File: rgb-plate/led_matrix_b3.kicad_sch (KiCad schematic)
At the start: 32 parts

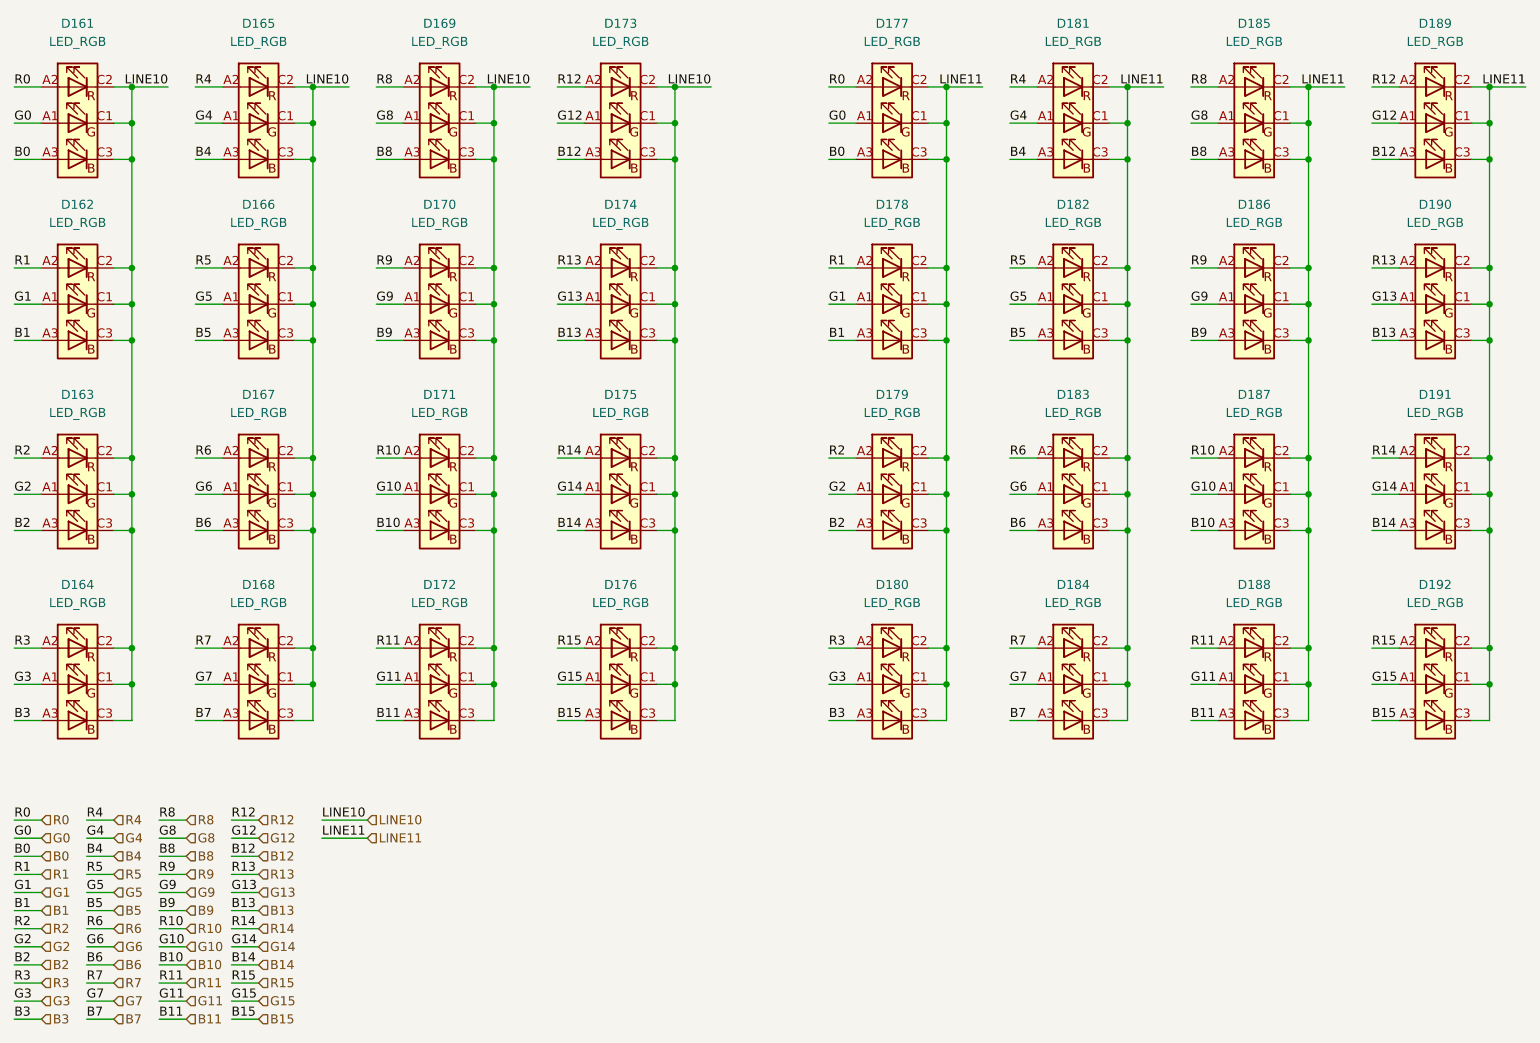
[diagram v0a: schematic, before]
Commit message: initial layout on single board, may need to split up
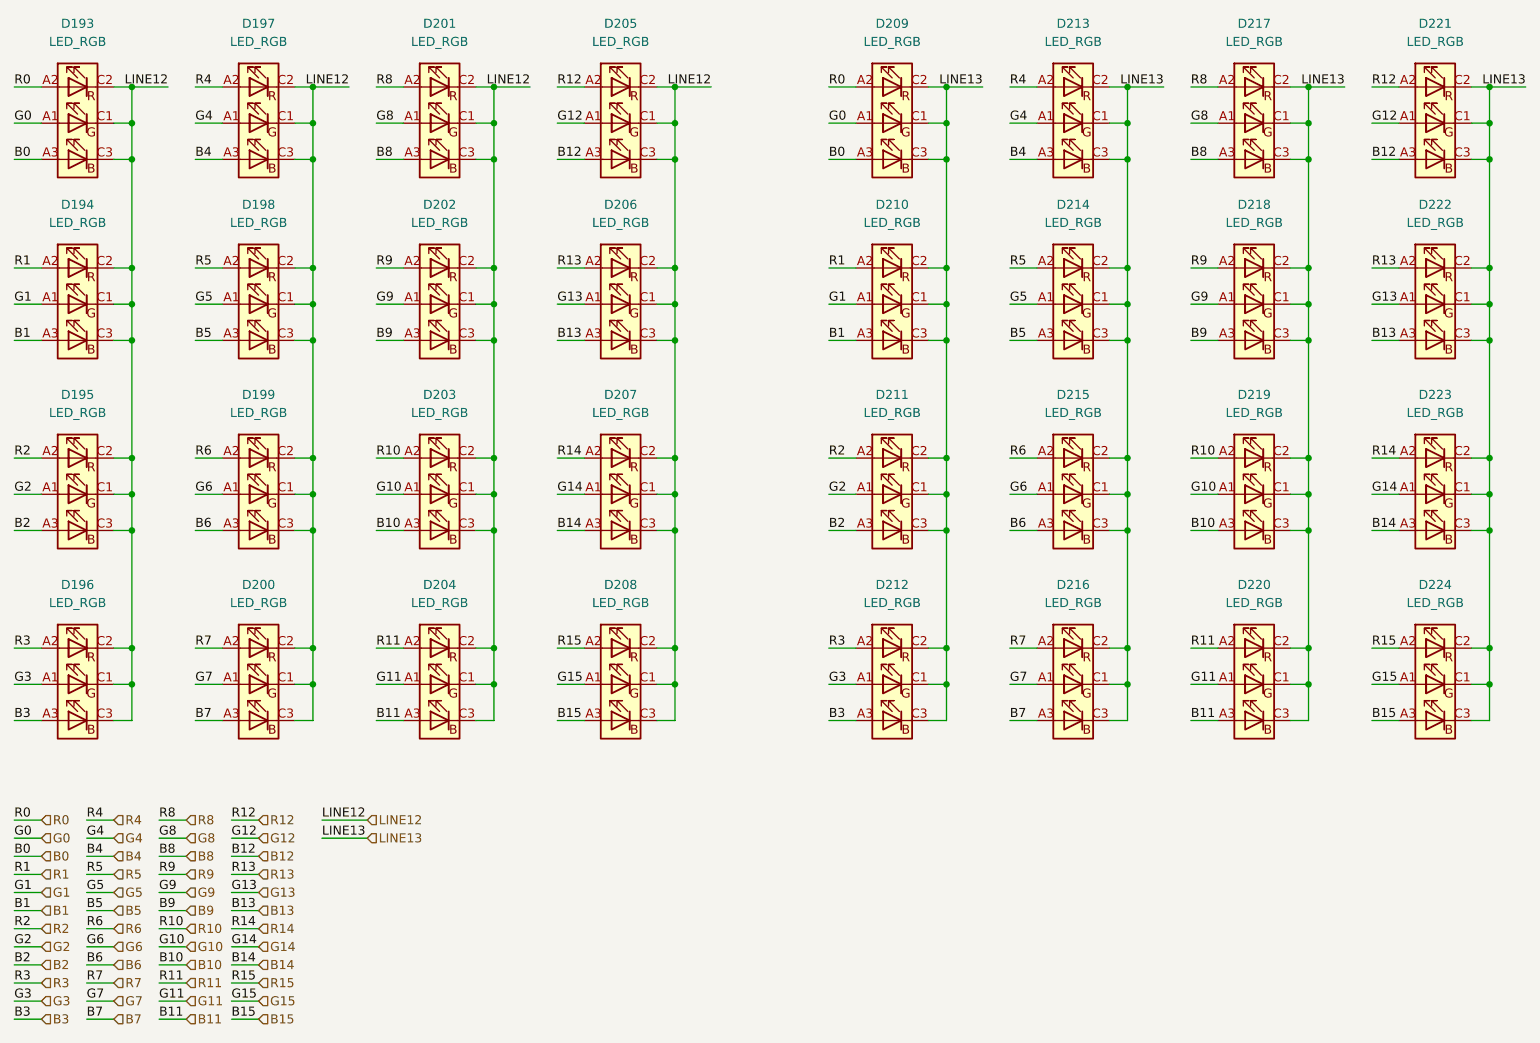
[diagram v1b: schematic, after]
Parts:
- removed D161, D162, D163, D164, D165, D166, D167, D168, D169, D170, D171, D172, D173, D174, D175, D176, D177, D178, D179, D180, D181, D182, D183, D184, D185, D186, D187, D188, D189, D190, D191, D192: LED_RGB, LRTBGVSR-4U4V-JW+8A8B-D8-3S4U-7Z:LRTBGVSR4U4VJW8A8BD83S4U7Z, symbol LRTBGVSR-4U4V-JW+8A8B-D8-3S4U-:LED_RGB
- added D193, D194, D195, D196, D197, D198, D199, D200, D201, D202, D203, D204, D205, D206, D207, D208, D209, D210, D211, D212, D213, D214, D215, D216, D217, D218, D219, D220, D221, D222, D223, D224: LED_RGB, LRTBGVSR-4U4V-JW+8A8B-D8-3S4U-7Z:LRTBGVSR4U4VJW8A8BD83S4U7Z, symbol LRTBGVSR-4U4V-JW+8A8B-D8-3S4U-:LED_RGB
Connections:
- net B0: now also D193.A3 (BA), D209.A3 (BA)
- net B1: now also D194.A3 (BA), D210.A3 (BA)
- net B10: now also D203.A3 (BA), D219.A3 (BA)
- net B11: now also D204.A3 (BA), D220.A3 (BA)
- net B12: now also D205.A3 (BA), D221.A3 (BA)
- net B13: now also D206.A3 (BA), D222.A3 (BA)
- net B14: now also D207.A3 (BA), D223.A3 (BA)
- net B15: now also D208.A3 (BA), D224.A3 (BA)
- net B2: now also D195.A3 (BA), D211.A3 (BA)
- net B3: now also D196.A3 (BA), D212.A3 (BA)
- net B4: now also D197.A3 (BA), D213.A3 (BA)
- net B5: now also D198.A3 (BA), D214.A3 (BA)
- net B6: now also D199.A3 (BA), D215.A3 (BA)
- net B7: now also D200.A3 (BA), D216.A3 (BA)
- net B8: now also D201.A3 (BA), D217.A3 (BA)
- net B9: now also D202.A3 (BA), D218.A3 (BA)
- net G0: now also D193.A1 (GA), D209.A1 (GA)
- net G1: now also D194.A1 (GA), D210.A1 (GA)
- net G10: now also D203.A1 (GA), D219.A1 (GA)
- net G11: now also D204.A1 (GA), D220.A1 (GA)
- net G12: now also D205.A1 (GA), D221.A1 (GA)
- net G13: now also D206.A1 (GA), D222.A1 (GA)
- net G14: now also D207.A1 (GA), D223.A1 (GA)
- net G15: now also D208.A1 (GA), D224.A1 (GA)
- net G2: now also D195.A1 (GA), D211.A1 (GA)
- net G3: now also D196.A1 (GA), D212.A1 (GA)
- net G4: now also D197.A1 (GA), D213.A1 (GA)
- net G5: now also D198.A1 (GA), D214.A1 (GA)
- net G6: now also D199.A1 (GA), D215.A1 (GA)
- net G7: now also D200.A1 (GA), D216.A1 (GA)
- net G8: now also D201.A1 (GA), D217.A1 (GA)
- net G9: now also D202.A1 (GA), D218.A1 (GA)
- net R0: now also D193.A2 (RA), D209.A2 (RA)
- net R1: now also D194.A2 (RA), D210.A2 (RA)
- net R10: now also D203.A2 (RA), D219.A2 (RA)
- net R11: now also D204.A2 (RA), D220.A2 (RA)
- net R12: now also D205.A2 (RA), D221.A2 (RA)
- net R13: now also D206.A2 (RA), D222.A2 (RA)
- net R14: now also D207.A2 (RA), D223.A2 (RA)
- net R15: now also D208.A2 (RA), D224.A2 (RA)
- net R2: now also D195.A2 (RA), D211.A2 (RA)
- net R3: now also D196.A2 (RA), D212.A2 (RA)
- net R4: now also D197.A2 (RA), D213.A2 (RA)
- net R5: now also D198.A2 (RA), D214.A2 (RA)
- net R6: now also D199.A2 (RA), D215.A2 (RA)
- net R7: now also D200.A2 (RA), D216.A2 (RA)
- net R8: now also D201.A2 (RA), D217.A2 (RA)
- net R9: now also D202.A2 (RA), D218.A2 (RA)
- new net LINE12: D193.C1 (GK), D193.C2 (RK), D193.C3 (BK), D194.C1 (GK), D194.C2 (RK), D194.C3 (BK), D195.C1 (GK), D195.C2 (RK), D195.C3 (BK), D196.C1 (GK), D196.C2 (RK), D196.C3 (BK), D197.C1 (GK), D197.C2 (RK), D197.C3 (BK), D198.C1 (GK), D198.C2 (RK), D198.C3 (BK), D199.C1 (GK), D199.C2 (RK), D199.C3 (BK), D200.C1 (GK), D200.C2 (RK), D200.C3 (BK), D201.C1 (GK), D201.C2 (RK), D201.C3 (BK), D202.C1 (GK), D202.C2 (RK), D202.C3 (BK), D203.C1 (GK), D203.C2 (RK), D203.C3 (BK), D204.C1 (GK), D204.C2 (RK), D204.C3 (BK), D205.C1 (GK), D205.C2 (RK), D205.C3 (BK), D206.C1 (GK), D206.C2 (RK), D206.C3 (BK), D207.C1 (GK), D207.C2 (RK), D207.C3 (BK), D208.C1 (GK), D208.C2 (RK), D208.C3 (BK)
- new net LINE13: D209.C1 (GK), D209.C2 (RK), D209.C3 (BK), D210.C1 (GK), D210.C2 (RK), D210.C3 (BK), D211.C1 (GK), D211.C2 (RK), D211.C3 (BK), D212.C1 (GK), D212.C2 (RK), D212.C3 (BK), D213.C1 (GK), D213.C2 (RK), D213.C3 (BK), D214.C1 (GK), D214.C2 (RK), D214.C3 (BK), D215.C1 (GK), D215.C2 (RK), D215.C3 (BK), D216.C1 (GK), D216.C2 (RK), D216.C3 (BK), D217.C1 (GK), D217.C2 (RK), D217.C3 (BK), D218.C1 (GK), D218.C2 (RK), D218.C3 (BK), D219.C1 (GK), D219.C2 (RK), D219.C3 (BK), D220.C1 (GK), D220.C2 (RK), D220.C3 (BK), D221.C1 (GK), D221.C2 (RK), D221.C3 (BK), D222.C1 (GK), D222.C2 (RK), D222.C3 (BK), D223.C1 (GK), D223.C2 (RK), D223.C3 (BK), D224.C1 (GK), D224.C2 (RK), D224.C3 (BK)
